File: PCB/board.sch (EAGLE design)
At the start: 24 parts, among them IC1 MEGA1284P-SQUARE, IC2 MC33269D-3.3, J1 DCJ0202, Q1 CRYSTAL_16MHZ_SMD, Q2 BUZ10, U1 OPA564AIDWD

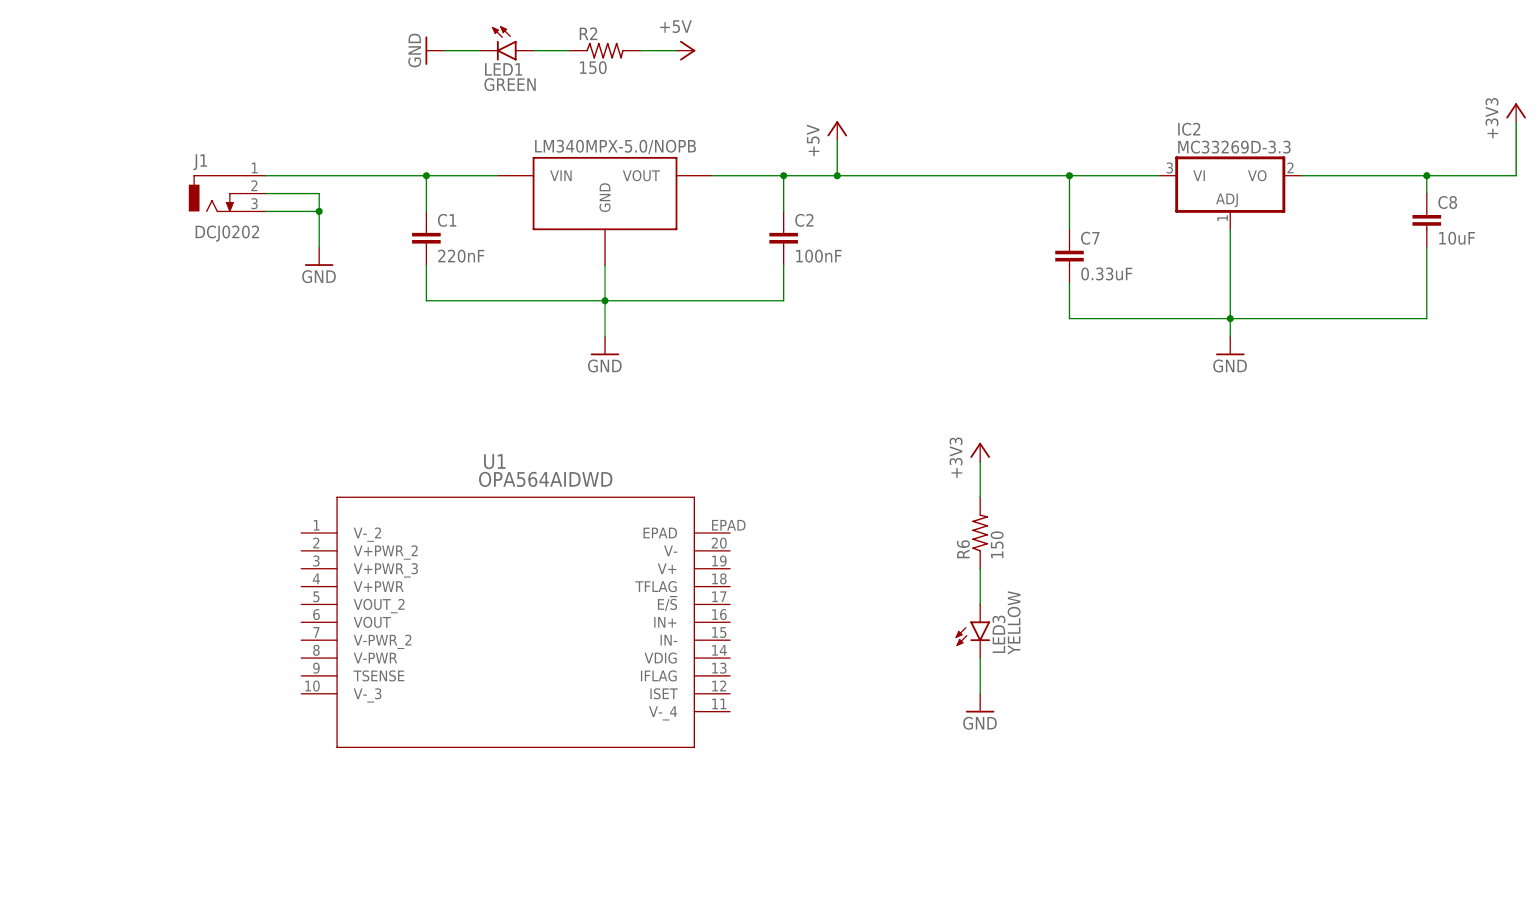
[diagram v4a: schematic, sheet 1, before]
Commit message: Finished connections for op-amp
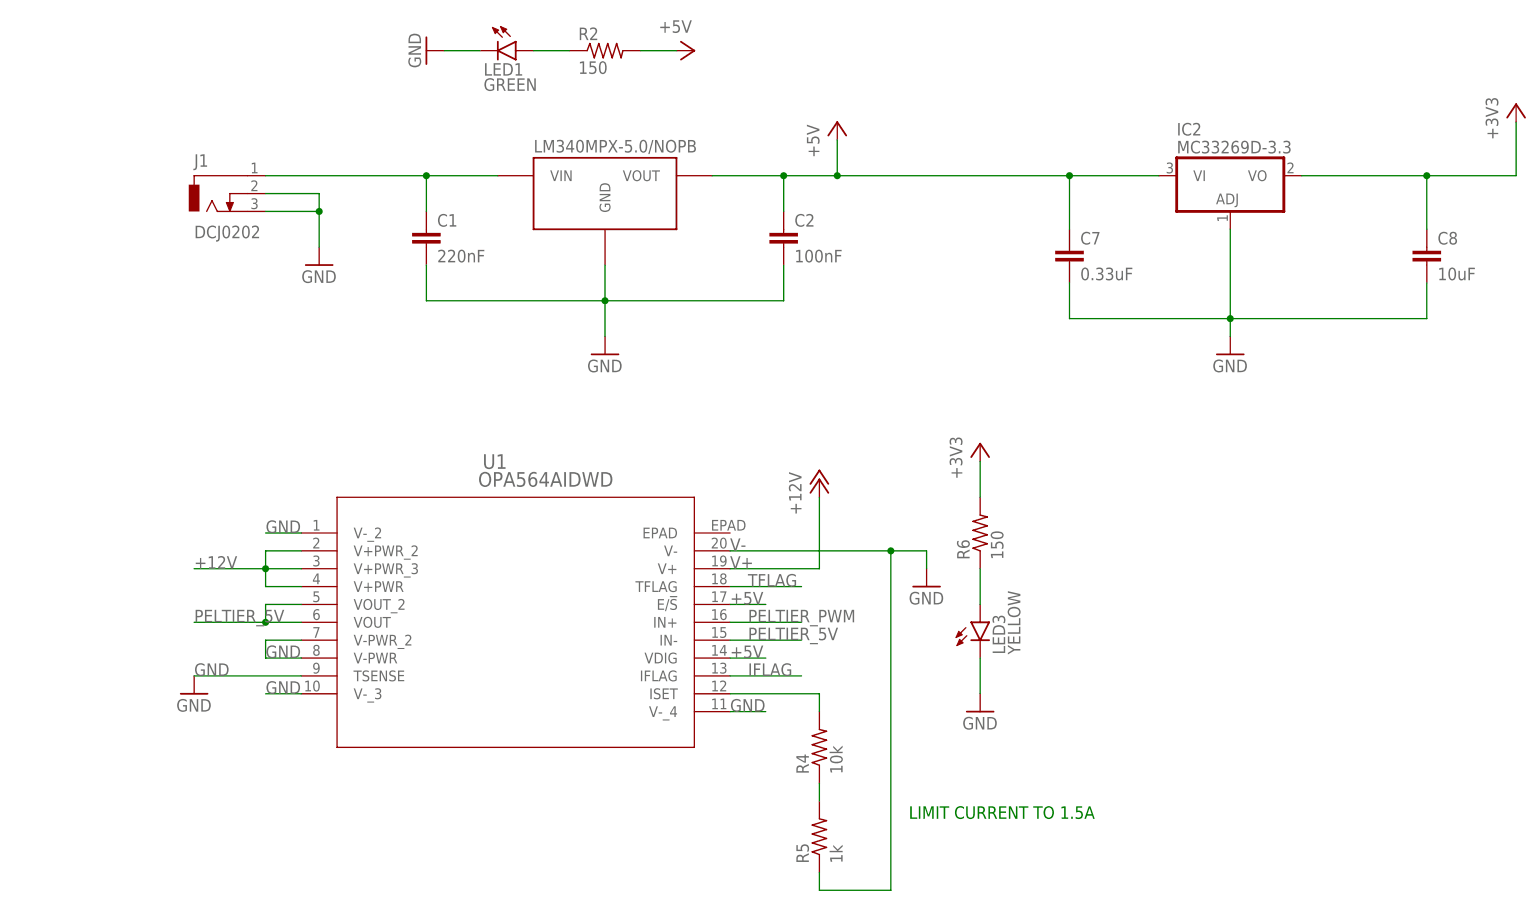
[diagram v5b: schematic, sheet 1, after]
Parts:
- added R4: 10k, rcl:R-US_R0603
- added R5: 1k, rcl:R-US_R0603
- U1: device myLibrary:OPA564AIDWD -> op-amp-library:OPA564AIDWD
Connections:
- removed net N$23: IC1.ADC0/PCINT0
- removed net N$24: IC1.ADC1/PCINT1
- new net IFLAG: IC1.ADC1/PCINT1, U1.IFLAG
- new net N$21: R4.1, R5.2
- new net N$7: R4.2, U1.ISET
- new net PELTIER_5V: U1.IN-, U1.VOUT, U1.VOUT_2
- new net TFLAG: IC1.ADC0/PCINT0, U1.TFLAG
- new net V+: U1.V+
- new net V-: R5.1, U1.V-
- net +12V: now also U1.V+PWR, U1.V+PWR_2, U1.V+PWR_3
- net +5V: now also U1.E/!S, U1.VDIG
- net GND: now also U1.TSENSE, U1.V-PWR, U1.V-PWR_2, U1.V-_2, U1.V-_3, U1.V-_4
- net PELTIER_PWM: now also U1.IN+
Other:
- note added: "LIMIT CURRENT TO 1.5A"
- moved on the sheet: C8

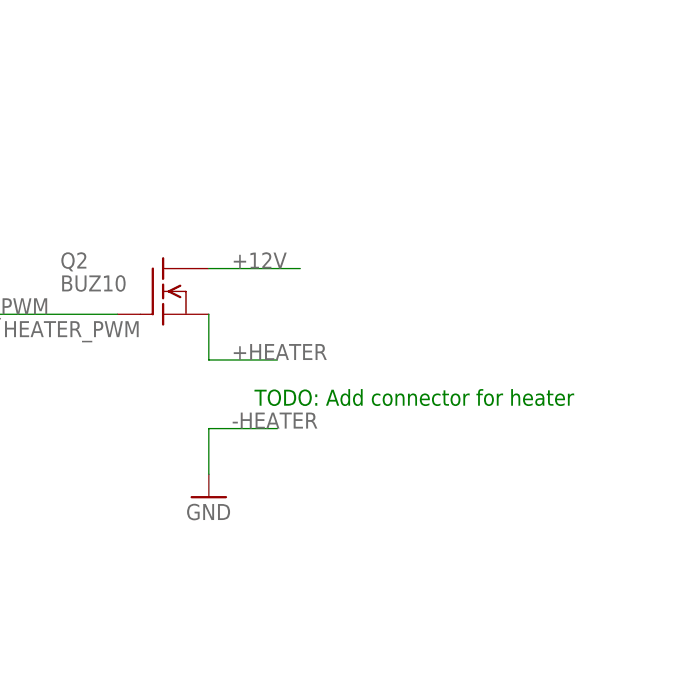
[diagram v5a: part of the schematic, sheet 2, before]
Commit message: Fixed mosfet
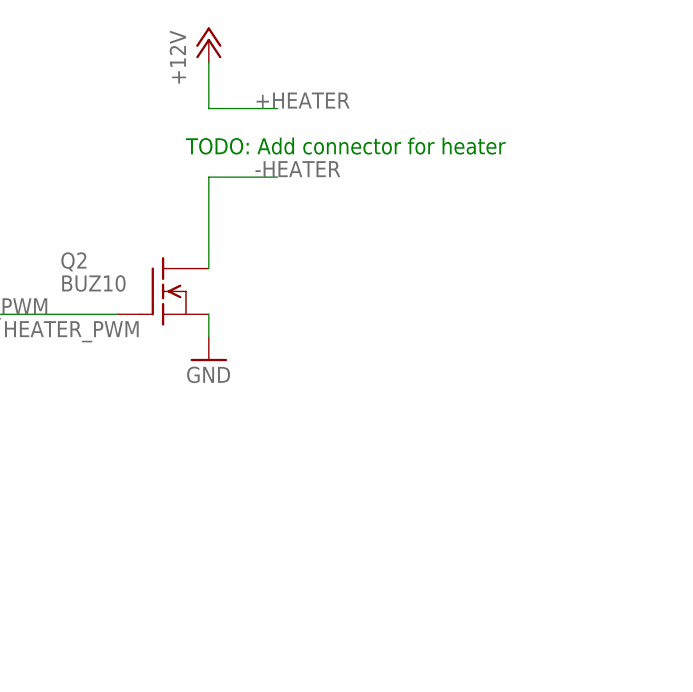
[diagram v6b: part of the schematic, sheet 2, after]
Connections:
- removed net +HEATER: Q2.S
- new net -HEATER: Q2.D
- net +12V: no longer Q2.D
- net GND: now also Q2.S
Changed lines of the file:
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@@
 <part name="U1" library="op-amp-library" deviceset="OPA564AIDWD" device=""/>
 <part name="GND13" library="supply1" library_urn="urn:adsk.eagle:library:371" deviceset="GND" device=""/>
+<part name="P+8" library="supply1" library_urn="urn:adsk.eagle:library:371" deviceset="+12V" device=""/>
 </parts>
 <sheets>
@@
 <sheet>
 <plain>
-<text x="210.82" y="114.3" size="1.778" layer="91">TODO: Add connector for heater</text>
+<text x="203.2" y="142.24" size="1.778" layer="91">TODO: Add connector for heater</text>
 </plain>
 <instances>
@@
 <attribute name="NAME" x="189.23" y="129.54" size="1.778" layer="95"/>
 </instance>
-<instance part="GND11" gate="1" x="205.74" y="104.14" smashed="yes">
-<attribute name="VALUE" x="203.2" y="101.6" size="1.778" layer="96"/>
+<instance part="GND11" gate="1" x="205.74" y="119.38" smashed="yes">
+<attribute name="VALUE" x="203.2" y="116.84" size="1.778" layer="96"/>
+</instance>
+<instance part="P+8" gate="1" x="205.74" y="154.94" smashed="yes">
+<attribute name="VALUE" x="203.2" y="149.86" size="1.778" layer="96" rot="R90"/>
 </instance>
 </instances>
@@
 <pinref part="GND10" gate="1" pin="GND"/>
 <wire x1="195.58" y1="25.4" x2="195.58" y2="20.32" width="0.1524" layer="91"/>
+</segment>
+<segment>
+<pinref part="GND11" gate="1" pin="GND"/>
+<pinref part="Q2" gate="G$1" pin="S"/>
+<wire x1="205.74" y1="121.92" x2="205.74" y2="124.46" width="0.1524" layer="91"/>
 </segment>
 </net>
@@
 </segment>
 </net>
-<net name="+12V" class="0">
+<net name="-HEATER" class="0">
 <segment>
 <pinref part="Q2" gate="G$1" pin="D"/>
-<wire x1="205.74" y1="129.54" x2="215.9" y2="129.54" width="0.1524" layer="91"/>
-<label x="208.28" y="129.54" size="1.778" layer="95"/>
+<wire x1="205.74" y1="129.54" x2="205.74" y2="139.7" width="0.1524" layer="91"/>
+<wire x1="205.74" y1="139.7" x2="213.36" y2="139.7" width="0.1524" layer="91"/>
+<label x="210.82" y="139.7" size="1.778" layer="95"/>
 </segment>
 </net>
 <net name="+HEATER" class="0">
 <segment>
-<pinref part="Q2" gate="G$1" pin="S"/>
-<wire x1="205.74" y1="124.46" x2="205.74" y2="119.38" width="0.1524" layer="91"/>
-<wire x1="205.74" y1="119.38" x2="213.36" y2="119.38" width="0.1524" layer="91"/>
-<label x="208.28" y="119.38" size="1.778" layer="95"/>
-</segment>
-</net>
-<net name="-HEATER" class="0">
-<segment>
-<pinref part="GND11" gate="1" pin="GND"/>
-<wire x1="205.74" y1="106.68" x2="205.74" y2="111.76" width="0.1524" layer="91"/>
-<wire x1="205.74" y1="111.76" x2="213.36" y2="111.76" width="0.1524" layer="91"/>
-<label x="208.28" y="111.76" size="1.778" layer="95"/>
-</segment>
-</net>
+<wire x1="213.36" y1="147.32" x2="205.74" y2="147.32" width="0.1524" layer="91"/>
+<wire x1="205.74" y1="147.32" x2="205.74" y2="152.4" width="0.1524" layer="91"/>
+<pinref part="P+8" gate="1" pin="+12V"/>
+<label x="210.82" y="147.32" size="1.778" layer="95"/>
+</segment>
+</net>

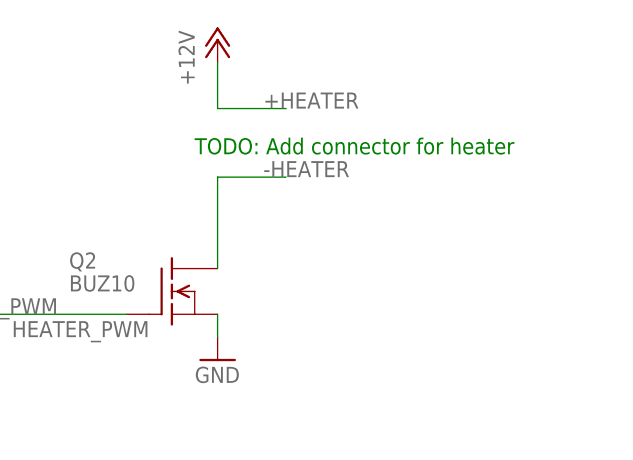
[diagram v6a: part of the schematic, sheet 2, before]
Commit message: Added connector for heater
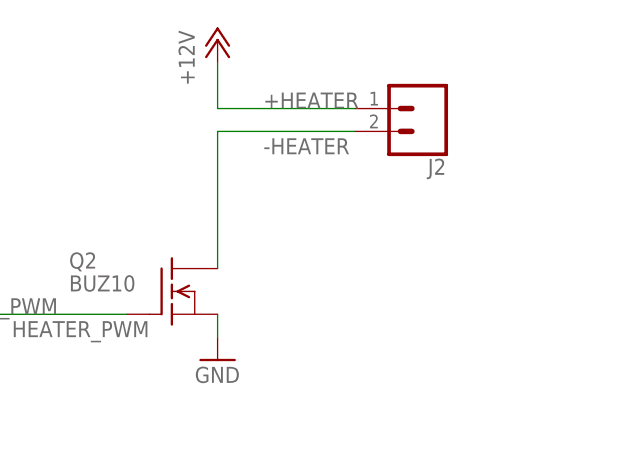
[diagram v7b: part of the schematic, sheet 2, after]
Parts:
- added J2: (no value), SparkFun-Connectors:CONN_025MM
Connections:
- removed net N$1: C1.1, J1.1, LDO1.VIN
- removed net V+: U1.V+
- removed net V-: R5.1, U1.V-
- new net +HEATER: J2.1
- net +12V: now also C1.1, J1.1, LDO1.VIN, U1.V+
- net -HEATER: now also J2.2
- net GND: now also R5.1, U1.V-
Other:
- note removed: "TODO: Add connector for heater"

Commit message: Placing on board
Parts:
- added PELTIER_CONNECTOR: (no value), SparkFun-Connectors:CONN_025MM
- added SV2, SV4: (no value), con-lstb:MA08-1
- added SV3: (no value), con-lstb:MA04-1
- added SV5: (no value), con-lstb:MA07-1
- renumbered J2 to HEATER_CONNECTOR
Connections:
- net N$7 renamed ISET
- net GND: now also PELTIER_CONNECTOR.2
- net IFLAG: now also SV2.2
- net N$10: now also SV5.5
- net N$11: now also SV5.4
- net N$12: now also SV5.3
- net N$13: now also SV5.2
- net N$14: now also SV5.1
- net N$15: now also SV4.8
- net N$16: now also SV4.7
- net N$17: now also SV4.6
- net N$18: now also SV4.5
- net N$19: now also SV4.4
- net N$20: now also SV4.3
- net N$25: now also SV2.3
- net N$26: now also SV2.4
- net N$27: now also SV2.5
- net N$28: now also SV2.6
- net N$29: now also SV2.7
- net N$30: now also SV2.8
- net N$31: now also SV3.1
- net N$32: now also SV3.2
- net N$33: now also SV3.3
- net N$35: now also SV3.4
- net N$8: now also SV5.7
- net N$9: now also SV5.6
- net PELTIER_5V: now also PELTIER_CONNECTOR.1
- net SCL: now also SV4.1
- net SDA: now also SV4.2
- net TFLAG: now also SV2.1
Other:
- moved on the sheet: SV1
